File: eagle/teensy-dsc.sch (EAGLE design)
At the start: 7 parts, among them M1 XBEERX-VN

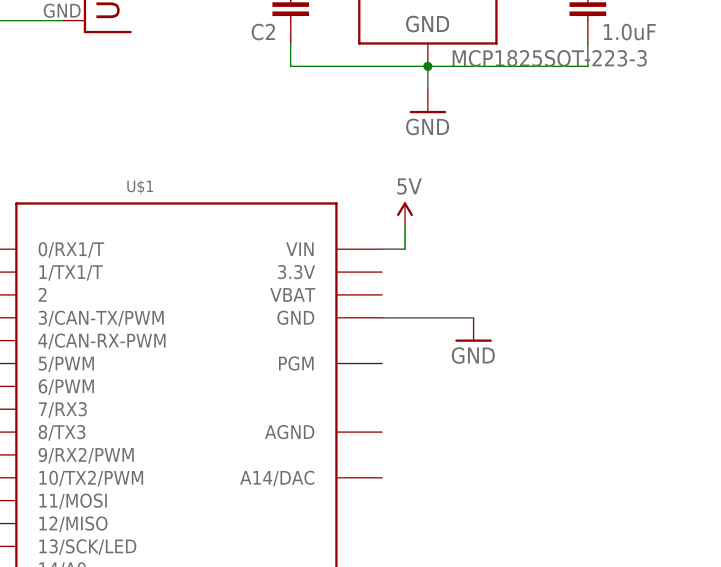
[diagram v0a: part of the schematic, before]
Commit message: updated with:
- latest WiFly board
- Thicker traces for routing 5V & GND
- Removed wiring for 3.3V on Teensy 3.1 board
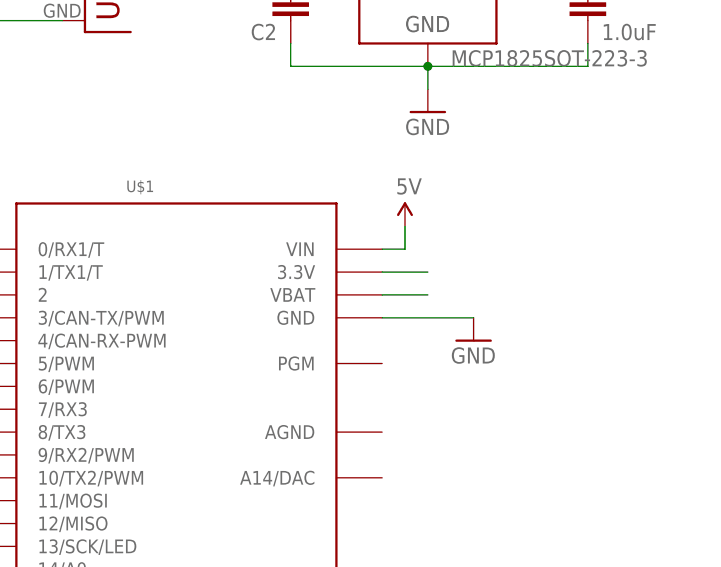
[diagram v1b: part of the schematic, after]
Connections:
- new net N$4: U$1.VBAT
- new net N$5: U$1.3.3V
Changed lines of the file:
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@@
+</segment>
+</net>
+<net name="N$4" class="0">
+<segment>
+<pinref part="U$1" gate="G$1" pin="VBAT"/>
+<wire x1="111.76" y1="71.12" x2="116.84" y2="71.12" width="0.1524" layer="91"/>
+</segment>
+</net>
+<net name="N$5" class="0">
+<segment>
+<pinref part="U$1" gate="G$1" pin="3.3V"/>
+<wire x1="111.76" y1="73.66" x2="116.84" y2="73.66" width="0.1524" layer="91"/>
 </segment>
 </net>

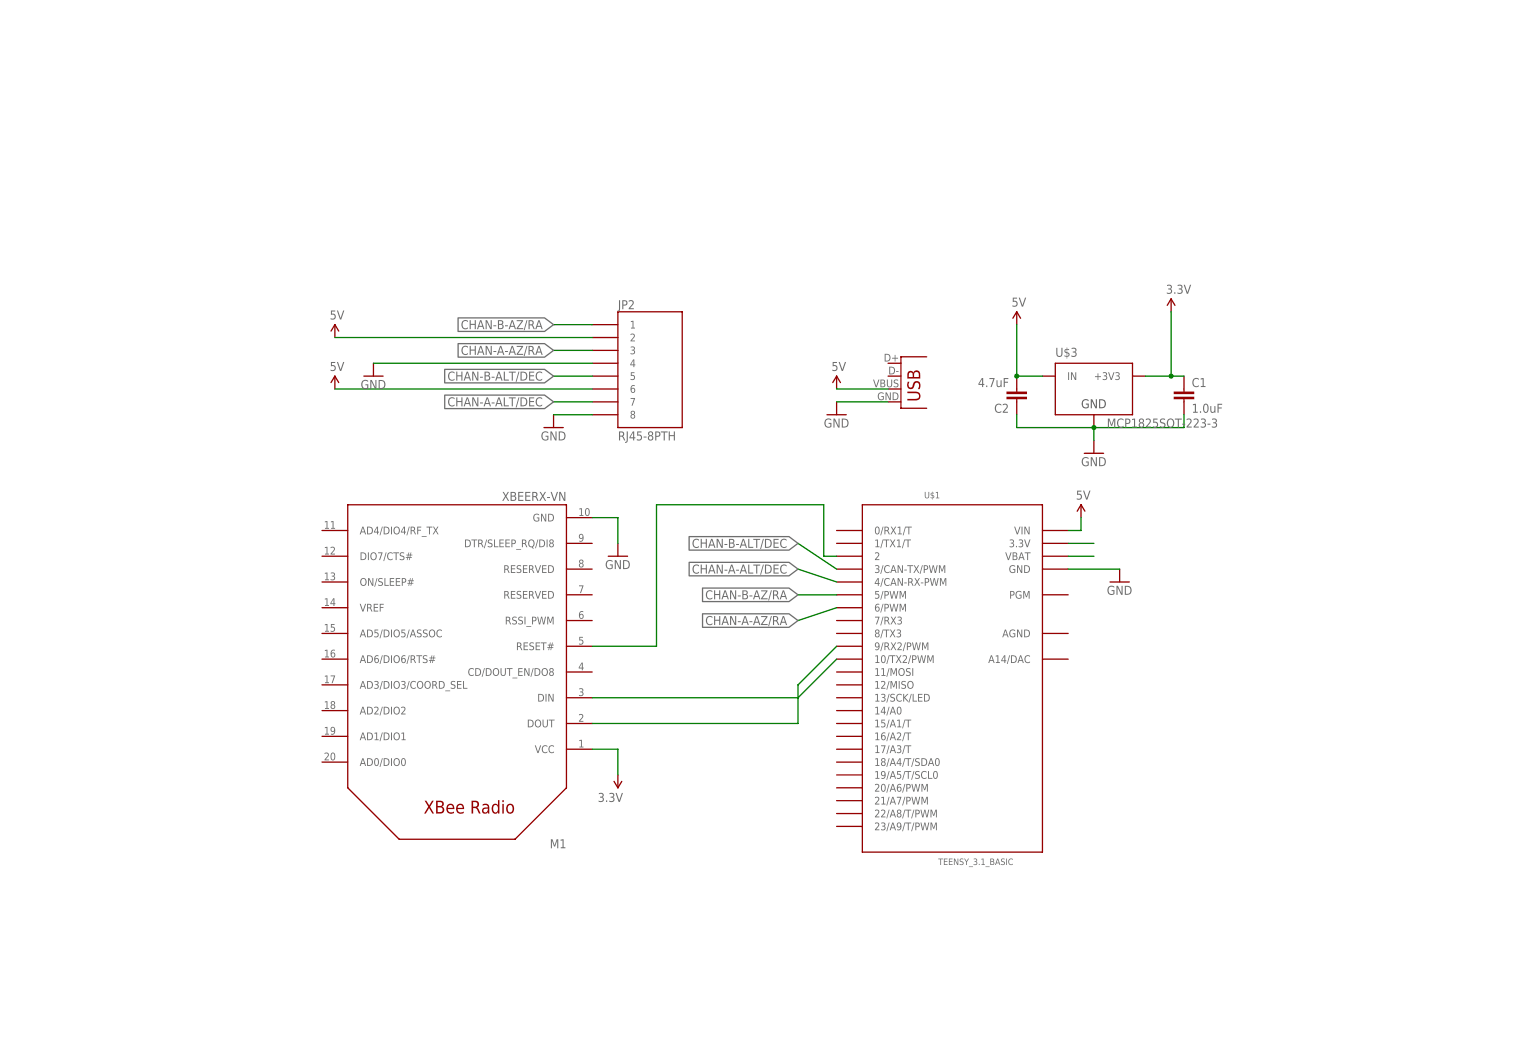
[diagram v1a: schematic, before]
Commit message: New board design: - Add 2x serial ports - Add camera trigger (opto-isolated) - Add 2x external button/switch - Add dedicated program button Remove old PCB design files Start work on TeensyDSC code
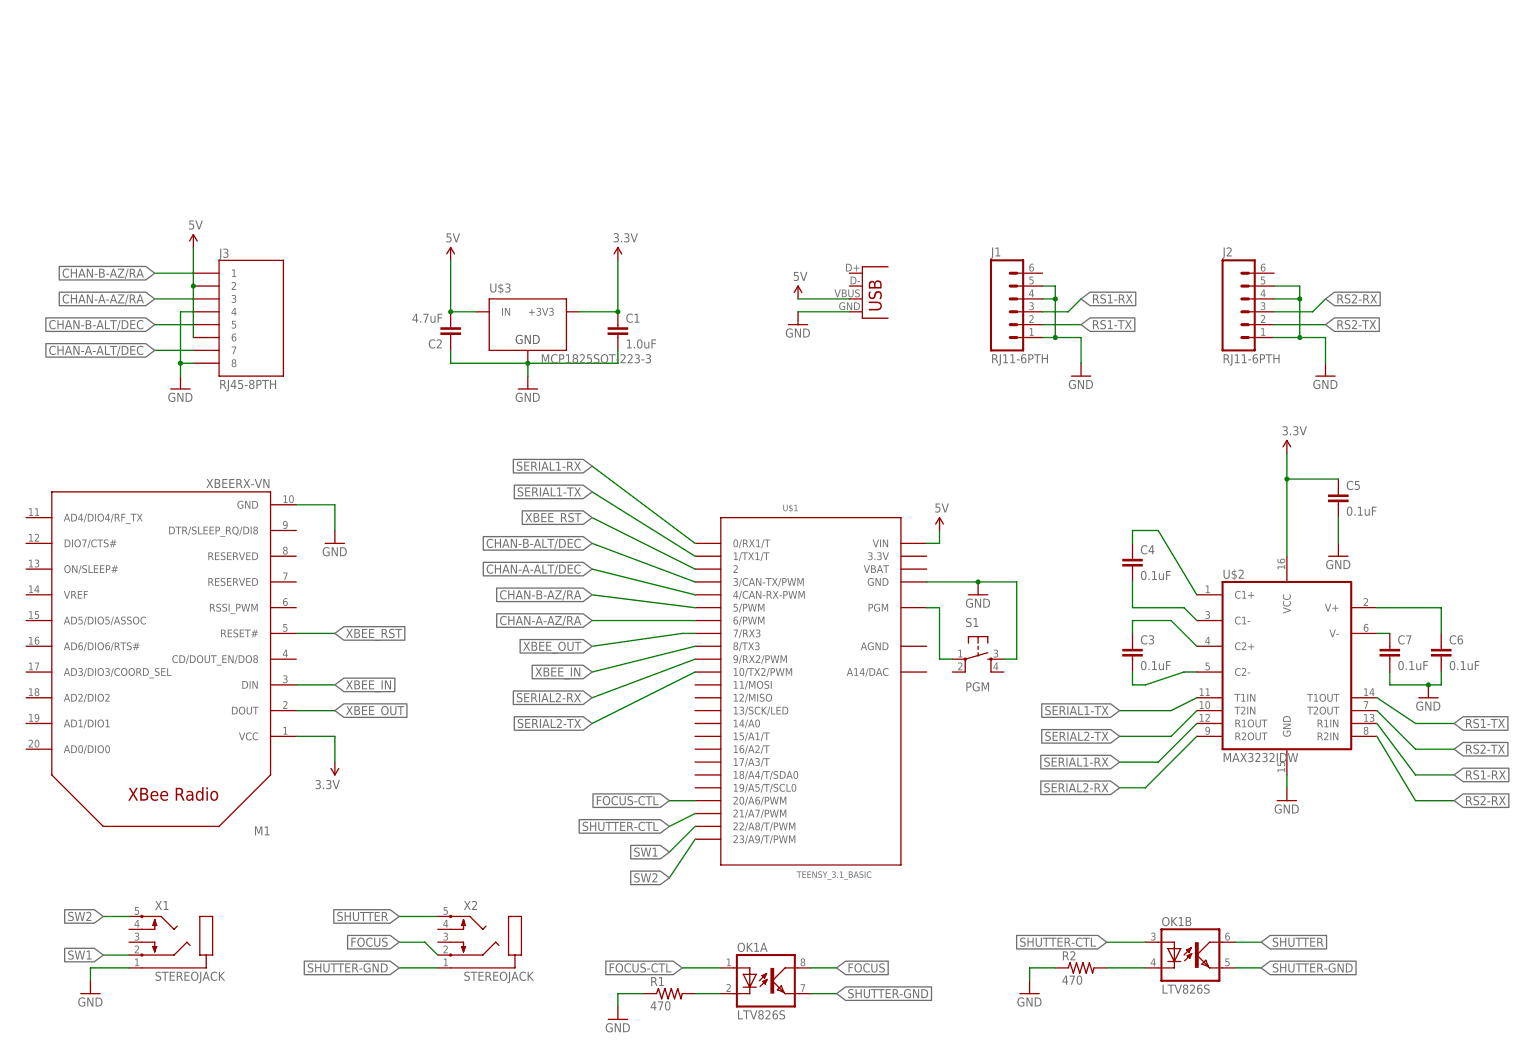
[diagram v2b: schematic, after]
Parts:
- removed JP2: RJ45-8PTH, SparkFun-Connectors:RJ45-8PTH
- added C3, C4, C5, C6, C7: 0.1uF, SparkFun-Passives:CAP0805
- added J1, J2: RJ11-6PTH, SparkFun-Connectors:RJ11-6PTH
- added J3: RJ45-8PTH, SparkFun-Connectors:RJ45-8PTH
- added OK1: LTV826S, optocoupler:LTV826S
- added R1, R2: 470, SparkFun-Resistors:0.75OHM1/4W1%(0805)
- added S1: PGM, SparkFun-Electromechanical:TAC_SWITCHPTH
- added U$2: MAX3232IDW, SparkFun-DigitalIC:MAX232SOIC16
- added X1, X2: STEREOJACK, adafruit:STEREOJACK
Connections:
- net N$3 renamed XBEE_RST
- new net FOCUS: OK1A.COL, X2.2
- new net FOCUS-CTL: OK1A.A, U$1.20/A6/PWM
- new net N$3: C3.1, U$2.C2+
- new net N$6: C6.1, U$2.V+
- new net N$7: OK1B.C, R2.2
- new net N$8: S1.1, U$1.PGM
- new net N$9: OK1A.C, R1.2
- new net RS1-RX: J1.3, U$2.R1IN
- new net RS1-TX: J1.2, U$2.T1OUT
- new net RS2-RX: J2.3, U$2.R2IN
- new net RS2-TX: J2.2, U$2.T2OUT
- new net SERIAL1-RX: U$1.0/RX1/T, U$2.R1OUT
- new net SERIAL1-TX: U$1.1/TX1/T, U$2.T1IN
- new net SERIAL2-RX: U$1.9/RX2/PWM, U$2.R2OUT
- new net SERIAL2-TX: U$1.10/TX2/PWM, U$2.T2IN
- new net SHUTTER: OK1B.COL, X2.5
- new net SHUTTER-CTL: OK1B.A, U$1.21/A7/PWM
- new net SHUTTER-GND: OK1A.EMIT, OK1B.EMIT, X2.1
- new net SW1: U$1.22/A8/T/PWM, X1.2
- new net SW2: U$1.23/A9/T/PWM, X1.5
- new net XBEE_IN: M1.DIN, U$1.8/TX3
- new net XBEE_OUT: M1.DOUT, U$1.7/RX3
- net 3.3V: now also C5.1, U$2.VCC
- net 5V: now also J3.2, J3.6; no longer JP2.2, JP2.6
- net CHAN-A-ALT/DEC: now also J3.7; no longer JP2.7
- net CHAN-A-AZ/RA: now also J3.3; no longer JP2.3
- net CHAN-B-ALT/DEC: now also J3.5; no longer JP2.5
- net CHAN-B-AZ/RA: now also J3.1; no longer JP2.1
- net GND: now also C5.2, C6.2, C7.2, J1.1, J1.4, J1.5, J2.1, J2.4, J2.5, J3.4, J3.8, R1.1, R2.1, S1.3, U$2.GND, X1.1; no longer JP2.4, JP2.8
- net N$1: now also C4.1, U$2.C1+; no longer M1.DIN, U$1.10/TX2/PWM
- net N$2: now also C4.2, U$2.C1-; no longer M1.DOUT, U$1.9/RX2/PWM
- net N$4: now also C3.2, U$2.C2-; no longer U$1.VBAT
- net N$5: now also C7.1, U$2.V-; no longer U$1.3.3V
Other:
- moved on the sheet: C1, C2, M1, U$1, U$3

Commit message: Mark board v0.2 Add a warning so people don't think it's ready for prime-time.
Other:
- note added: "TeensyDSC v0.2 http://synfin.net/teensydsc 20140908"
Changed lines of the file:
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@@
 <sheet>
 <plain>
+<text x="33.02" y="144.78" size="2.54" layer="90">TeensyDSC v0.2
+http://synfin.net/teensydsc
+20140908</text>
 </plain>
 <instances>
@@
 </schematic>
 </drawing>
+<compatibility>
+<note version="6.3" minversion="6.2.2" severity="warning">
+Since Version 6.2.2 text objects can contain more than one line,
+which will not be processed correctly with this version.
+</note>
+</compatibility>
 </eagle>

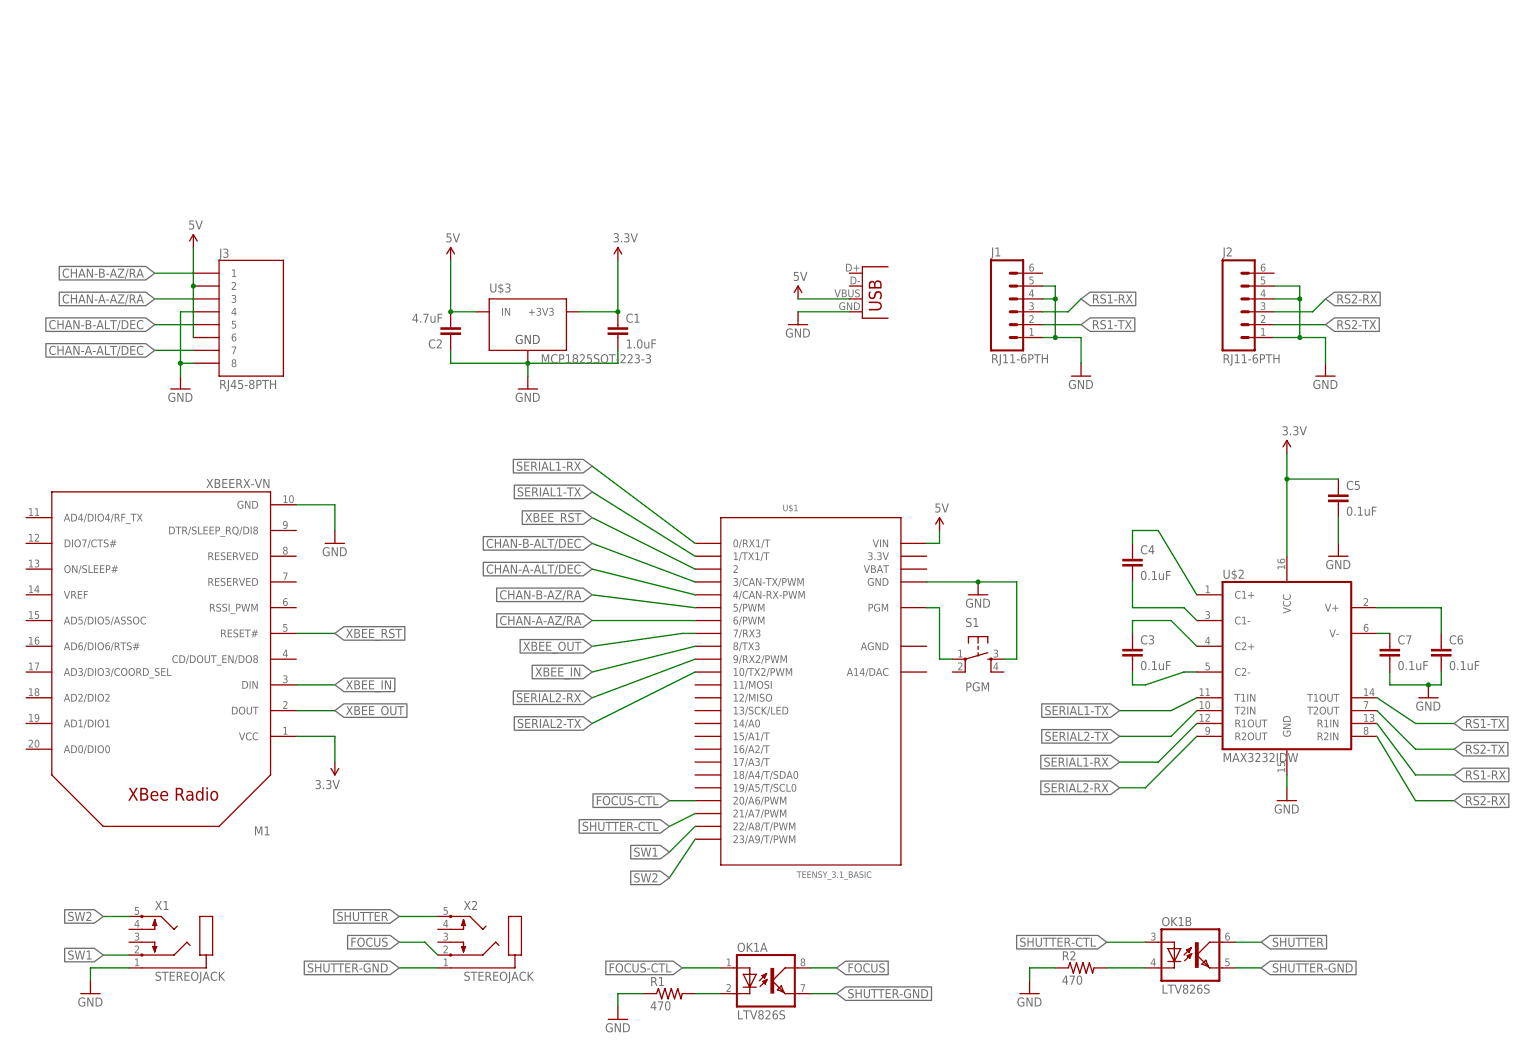
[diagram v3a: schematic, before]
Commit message: Update board design with: - Remove program button since USB host mode isn't supported - Add 5mm barrel connector for ~12V power - Add necessary reverse polarity protection & regulation for 12V power - Add a frame to the .sch file
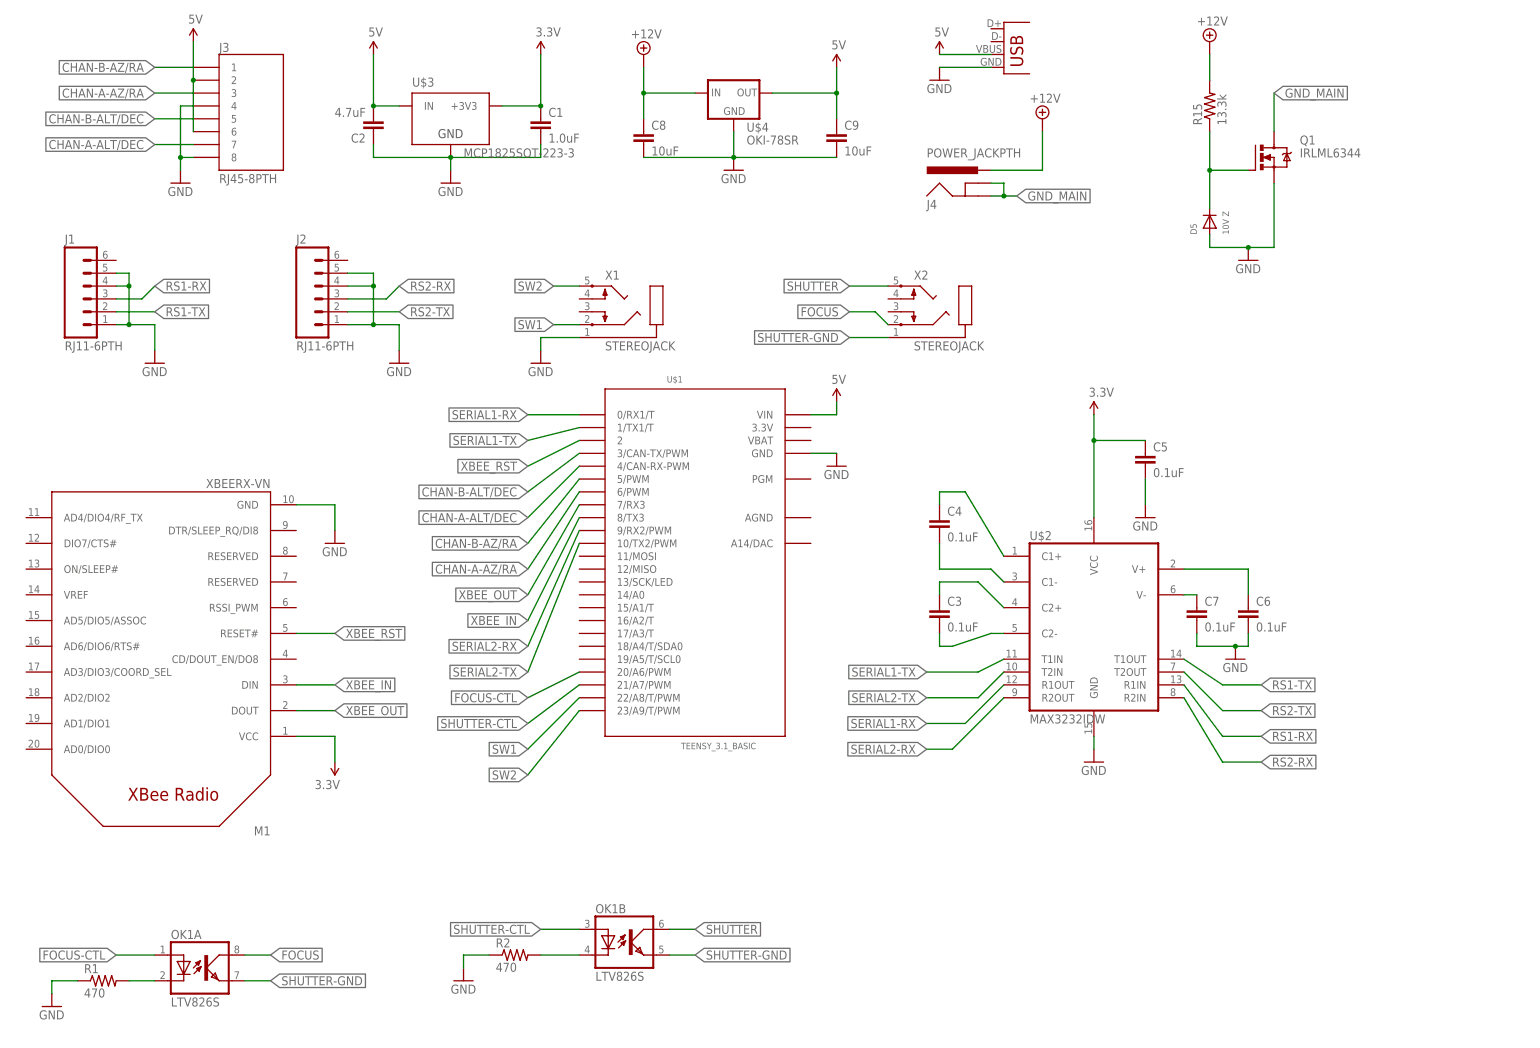
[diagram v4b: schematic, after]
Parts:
- removed S1: PGM, SparkFun-Electromechanical:TAC_SWITCHPTH
- added C8, C9: 10uF, resistor:C-EUC0805
- added D5: 10V Z, adafruit:DIODESOD-123
- added J4: POWER_JACKPTH, SparkFun-Connectors:POWER_JACKPTH
- added Q1: IRLML6344, synfinatic:IRLML6344
- added R15: 13.3k, resistor:R-US_M0805
- added U$4: OKI-78SR, synfinatic:OKI-78SR
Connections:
- removed net N$8: S1.1, U$1.PGM
- new net +12V: C8.1, J4.PWR, R15.2, U$4.IN
- new net GND_MAIN: J4.GND, J4.GNDBREAK, Q1.D
- new net N$17: D5.C, Q1.G, R15.1
- net 5V: now also C9.1, U$4.OUT
- net GND: now also C8.2, C9.2, D5.A, Q1.S, U$4.GND; no longer S1.3
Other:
- note added: "Aaron Turner http://synfin.net/teensydsc"
- note added: "v0.3"
- note removed: "TeensyDSC v0.2 http://synfin.net/teensydsc 20140908"
- moved on the sheet: C1, C2, C3, C4, C5, C6, C7, J1, J2, J3, OK1A, OK1B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
